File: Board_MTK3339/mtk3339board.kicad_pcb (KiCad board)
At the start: 2 copper layers, 30.5 x 19.2 mm, 9 parts, among them P1 CONN_02X05, Q1 BSS138, U1 MTK3339

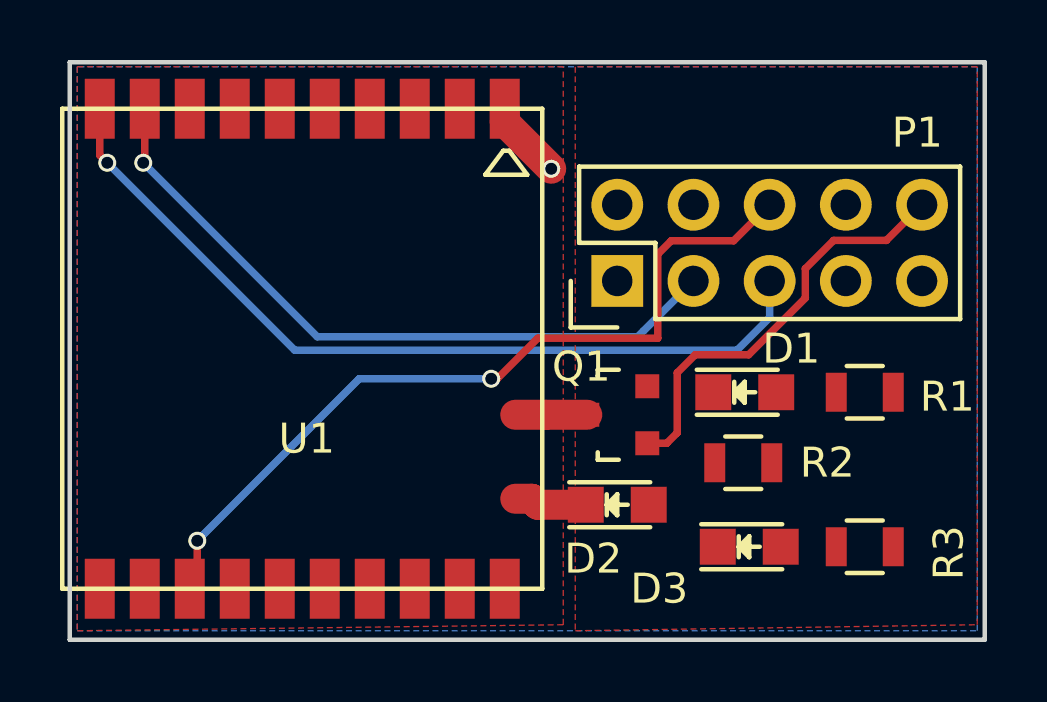
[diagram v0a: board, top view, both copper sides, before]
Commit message: updated baord for MTK3339 - should sit more correclty now
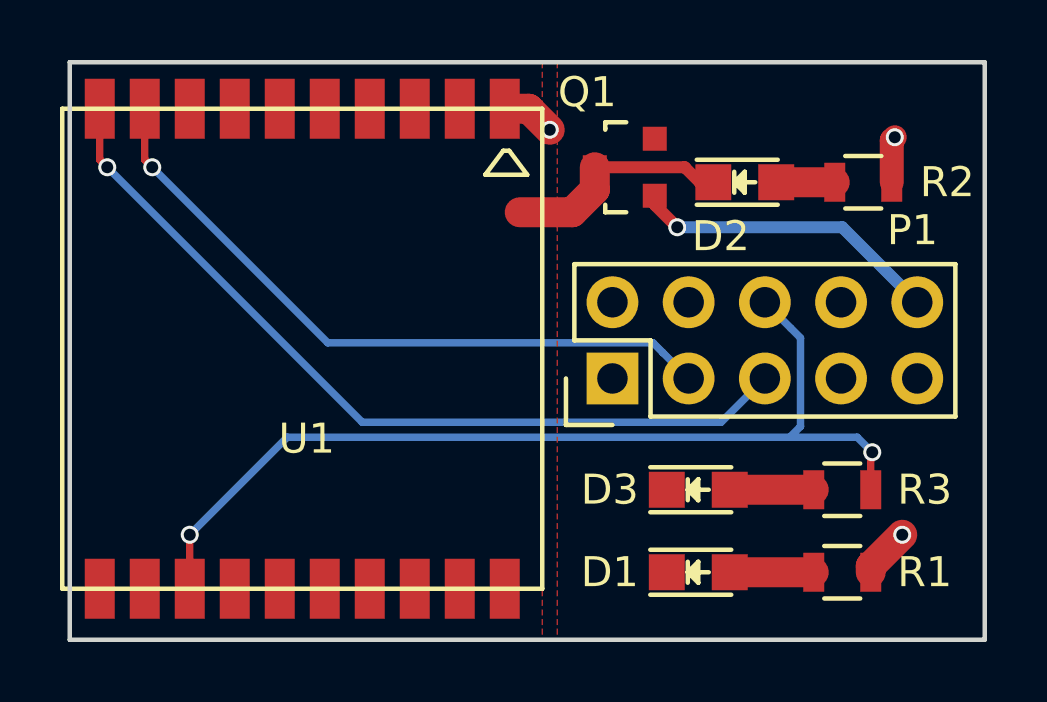
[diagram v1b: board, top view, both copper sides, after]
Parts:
- moved D2 11.6 mm to (141.2, 99.2)
- moved R2 10.2 mm to (145.2, 99.2)
- moved Q1 8.25 mm to (137.2, 98.8)
- moved D1 6.20 mm to (139.7, 112.2)
- moved R1 6.05 mm to (144.5, 112.2)
- moved P1 3.25 mm to (136.8, 105.8)
- moved D3 2.55 mm to (139.7, 109.5)
- moved R3 2.04 mm to (144.5, 109.5)
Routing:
- net GP_14: track 27.1 -> 32.5 mm
- net GP_17: track 14.2 -> 10.4 mm, vias 0 -> 1
- net GP_GND: track 4.84 -> 7.72 mm
- net Net-(D3-Pad2): track 0.00 -> 2.80 mm
- net Net-(D1-Pad2): track 0.00 -> 2.80 mm
- net +3V3: track 2.64 -> 5.02 mm, vias 1 -> 3
- net Net-(D2-Pad2): track 0.00 -> 1.95 mm
